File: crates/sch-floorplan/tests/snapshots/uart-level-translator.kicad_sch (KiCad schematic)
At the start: 11 parts, among them J1 Conn_01x05, U2 SN74LVC2T45DCUR

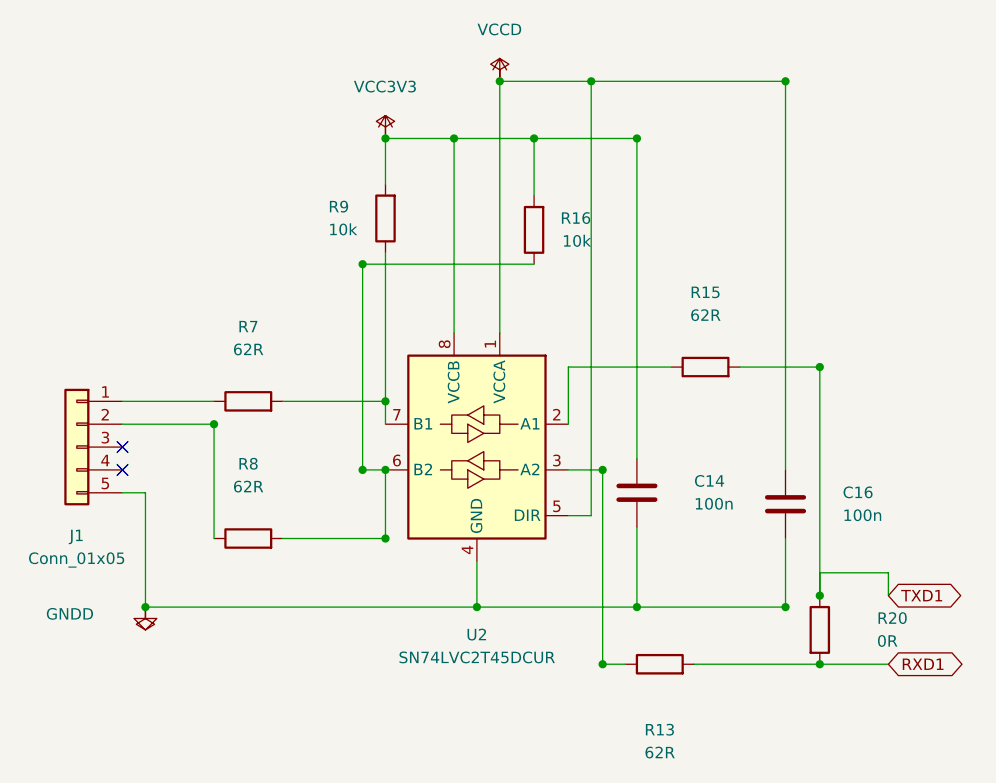
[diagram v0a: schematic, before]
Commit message: sch-doc: pick the smallest standard page from an A5-first ladder
A four-part circuit on A4 is a drawing stranded in one corner of an
empty sheet; the critic scored that a point worse than the snug custom
page it replaced. Starting the ladder at A5 keeps the frame close to
the content while every sheet still lands on a size KiCad and a printer
recognise.

Re-blessed the five snapshots whose critic score held at or above their
pre-change score. grid-demo is left at its baseline: it renders 7 where
it used to render 9.

Claude-Session: https://claude.ai/code/session_01GyGRY43X8yBh8WS1tjEmFz
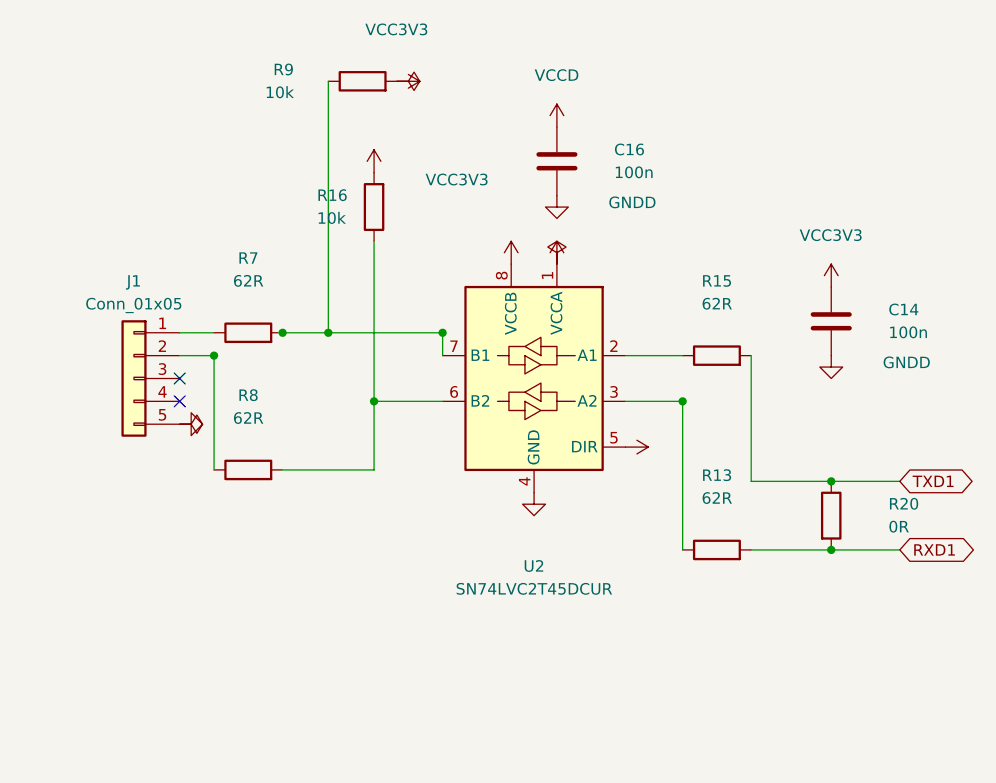
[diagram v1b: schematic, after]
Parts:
- C14, C16, J1, R13, R15, R16, R7, R8, R9, U2: ap_block (none) -> uart
- R20: ap_block (none) -> mcu
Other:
- moved on the sheet: C14, C16, J1, R13, R15, R16, R20, R7, R8, R9, U2
